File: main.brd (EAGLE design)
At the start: 43.4 x 29.3 mm, 26 parts, among them IC1 FT232RL, U1 ATMEGA328P_TQFP, Y3 16MHz

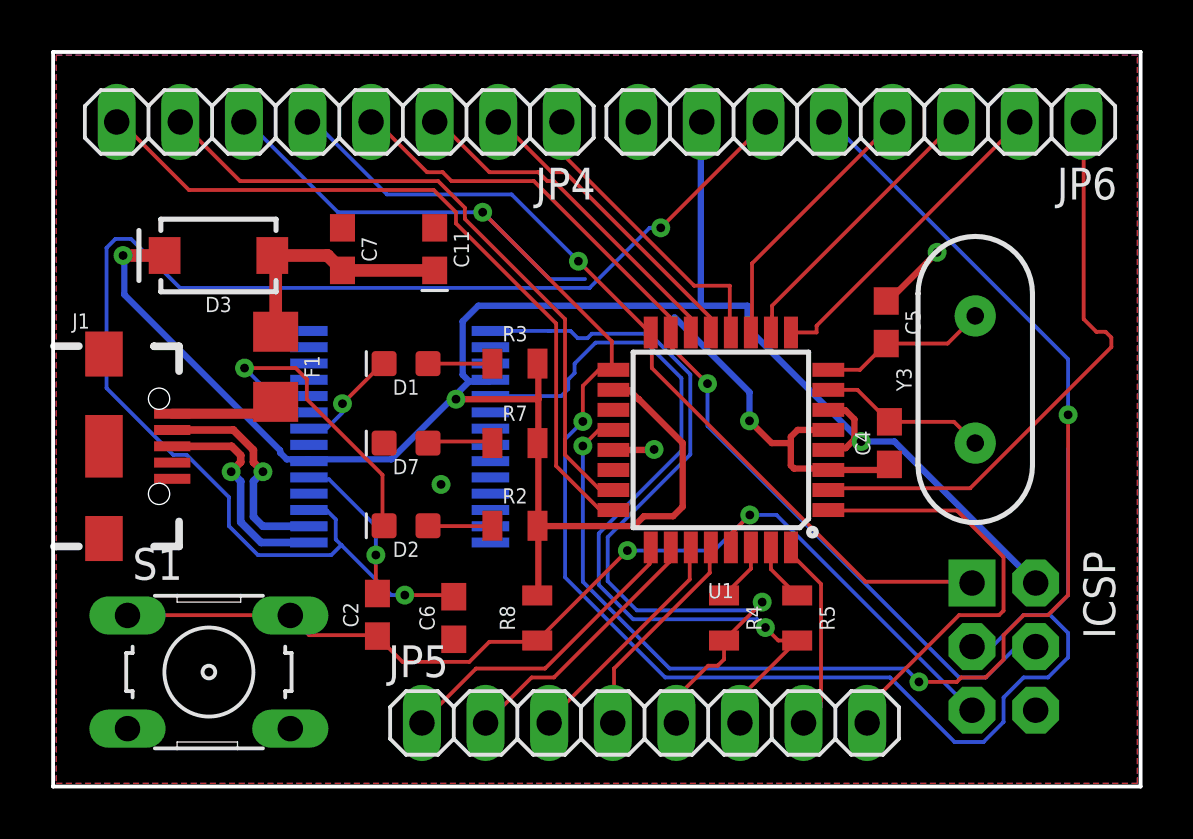
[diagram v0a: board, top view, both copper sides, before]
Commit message: 8/1/17 - Used new ATMEGA32U4
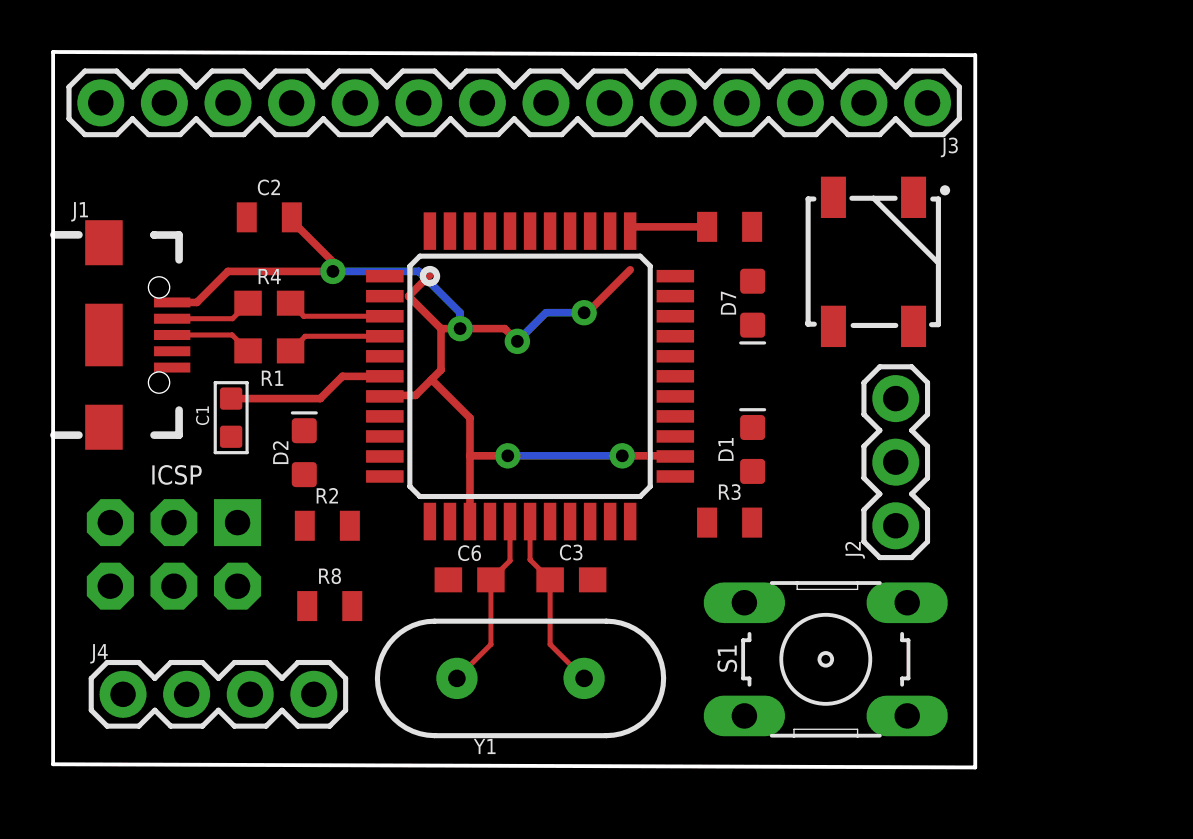
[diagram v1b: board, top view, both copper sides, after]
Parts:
- removed C11: 4.7uF, SparkFun-Capacitors:0603-POLAR
- removed C4, C5: 22pF, SparkFun-Capacitors:0603
- removed C7: 0.1uF, SparkFun-Capacitors:0603
- removed F1: 6V/0.5A, SparkFun-Fuses:1206
- removed IC1: FT232RL, ftdichip:SSOP28
- removed JP4, JP5, JP6: (no value), pinhead:1X08
- removed R5: 1k, SparkFun-Resistors:0805
- removed U1: ATMEGA328P_TQFP, SparkFun-IC-Microcontroller:TQFP32-08
- removed Y3: 16MHz, SparkFun-Clocks:HC49US
- added C1: 1uf, Seeed-Capacitor:C0603
- added C3: 22pF, SparkFun-Capacitors:0603
- added J2: (no value), SparkFun-Connectors:1X03
- added J3: (no value), SparkFun-Connectors:1X14
- added J4: (no value), SparkFun-Connectors:1X04
- added R1: 22, SparkFun-Resistors:0603
- added U$1: 32U4, SparkFun-IC-Microcontroller:TQFP44
- added Y1: 16MHz, SparkFun-Clocks:HC49US
- C2: value 0.1uF -> 10uF; device SparkFun-Capacitors:0603 -> SparkFun-Capacitors:0805
- C6: value 0.1uF -> 22pF
- D3: value 2A/100V/850mV -> WS2812B; device SparkFun-DiscreteSemi:SMA-DIODE -> SparkFun-LED:WS2812B
- R4: value 1k -> 22; device SparkFun-Resistors:0805 -> SparkFun-Resistors:0603
- moved ICSP 33.4 mm to (4.83, 11.9), turned to 180 degrees
- moved D3 26.2 mm to (32.8, 23.6), turned to 270 degrees
- moved S1 24.6 mm to (30.9, 7.75), turned to 180 degrees
- moved R4 22.1 mm to (8.64, 22.0), turned to 0 degrees
- moved C2 16.5 mm to (8.64, 25.4), turned to 0 degrees
- moved D7 14.9 mm to (27.9, 22.0), turned to 270 degrees
- moved D1 14.3 mm to (27.9, 16.1), turned to 90 degrees
- moved R7 12.2 mm to (27.0, 25.0), turned to 180 degrees
- moved R3 10.7 mm to (27.0, 13.2), turned to 180 degrees
- moved R8 8.30 mm to (11.0, 9.87), turned to 0 degrees
- moved R2 7.49 mm to (11.0, 13.1)
- moved D2 5.00 mm to (10.0, 16.0), turned to 90 degrees
- moved J1 4.45 mm to (2.03, 20.7)
- moved C6 1.65 mm to (16.6, 10.9), turned to 0 degrees
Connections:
- removed net 3.3V: C6.2, IC1.17, JP6.6
- removed net CBUS0: D2.C, IC1.23
- removed net CBUS1: D1.C, IC1.22
- removed net N$7: C2.2, IC1.19
- removed net PB0: JP4.1, U1.12
- removed net PB1: JP4.2, U1.13
- removed net PB2: JP4.3, U1.14
- removed net PC0: JP4.7, U1.23
- removed net PC1: JP4.8, U1.24
- removed net PC2: JP5.1, U1.25
- removed net PC3: JP5.2, U1.26
- removed net PC4: JP5.3, U1.27
- removed net PC5: JP5.4, U1.28
- removed net PD2: JP5.7, U1.32
- removed net PD3: JP5.8, U1.1
- removed net PD5: JP6.2, U1.9
- removed net RX_1_N: IC1.5, JP5.6, R5.2
- removed net RX_1_P: IC1.1, JP5.5, R4.2
- removed net VBUS: F1.2, J1.VBUS
- removed net V_USB: C11.+, C7.2, D3.A, F1.1
- new net PB4: J3.1, U$1.28
- new net PB5: D3.4, J3.2, U$1.29
- new net PB6: J3.3, U$1.30
- new net PB7: U$1.12
- new net PC6: J3.4, U$1.31
- new net PC7: J3.5, U$1.32
- new net PD0: J4.1, U$1.18
- new net PD1: J4.2, U$1.19
- new net PE6: U$1.1
- new net PF0: J3.11, U$1.41
- new net PF1: J3.10, U$1.40
- new net PF4: J3.9, U$1.39
- new net PF5: J3.8, U$1.38
- new net PF6: J3.7, U$1.37
- new net PF7: J3.6, U$1.36
- new net RX_LED: R2.2, U$1.8
- new net TX_LED: R3.2, U$1.22
- new net UCAP: C1.1, U$1.6
- new net USBD1_N: R4.2, U$1.3
- new net USBD1_P: R1.2, U$1.4
- net 5V: now also C2.2, D3.1, J1.VBUS, J3.14, U$1.14, U$1.2, U$1.24, U$1.34, U$1.44, U$1.7; no longer D3.C, IC1.20, IC1.4, JP6.7, R2.2, R3.2, U1.18, U1.4, U1.6
- net AREF: now also J3.12, U$1.42; no longer JP6.5, U1.20
- net GND: now also C1.2, C2.1, C3.1, D1.C, D2.C, D3.3, J3.13, U$1.15, U$1.23, U$1.33, U$1.35, U$1.43, U$1.5; no longer C11.-, C4.1, C5.1, C7.1, IC1.18, IC1.21, IC1.25, IC1.26, IC1.7, JP6.8, U1.21, U1.3, U1.5
- net MISO: now also U$1.11; no longer JP4.5, U1.16
- net MOSI: now also U$1.10; no longer JP4.4, U1.15
- net PD4: now also J2.1, U$1.25; no longer JP6.1, U1.2
- net PD6: now also J2.2, U$1.26; no longer JP6.3, U1.10
- net PD7: now also J2.3, U$1.27; no longer JP6.4, U1.11
- net RST: now also U$1.13; no longer C2.1, U1.29
- net RX_N: now also J4.4, U$1.21; no longer R5.1, U1.31
- net RX_P: now also J4.3, U$1.20; no longer R4.1, U1.30
- net SCK: now also U$1.9; no longer JP4.6, U1.17
- net USBD_N: now also R4.1; no longer IC1.16
- net USBD_P: now also R1.1; no longer IC1.15
- net XTAL_N: now also C6.2, U$1.16, Y1.2; no longer C5.2, U1.8, Y3.2
- net XTAL_P: now also C3.2, U$1.17, Y1.1; no longer C4.2, U1.7, Y3.1
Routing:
- net SCK: track 71.5 -> 0.00 mm, vias 2 -> 0
- net 3.3V: track 56.4 -> 0.00 mm, vias 2 -> 0
- net AREF: track 52.9 -> 0.00 mm, vias 3 -> 0
- net RST: track 41.8 -> 0.00 mm, vias 2 -> 0
- net 5V: track 88.8 -> 49.7 mm, vias 3 -> 6
- net MOSI: track 38.0 -> 0.00 mm, vias 1 -> 0
- net MISO: track 35.0 -> 0.00 mm, vias 1 -> 0
- net RX_1_P: track 32.3 -> 0.00 mm, vias 1 -> 0
- net RX_1_N: track 32.3 -> 0.00 mm, vias 1 -> 0
- net PC1: track 29.9 -> 0.00 mm
- net PC0: track 26.8 -> 0.00 mm
- net PD4: track 23.3 -> 0.00 mm
- net GND: track 18.8 -> 0.00 mm, vias 4 -> 0
- net PD3: track 17.6 -> 0.00 mm
- net PB2: track 14.1 -> 0.00 mm
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- removed copper zone on layer 1, net GND
- removed copper zone on layer 16, net GND
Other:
- board size 43.4 x 29.3 mm -> 36.8 x 28.6 mm

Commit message: Move vias
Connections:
- net RX_N renamed TX
- net RX_P renamed RX
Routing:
- net 5V: track 49.7 -> 54.7 mm, vias 6 -> 5
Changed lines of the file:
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@@
 <via x="11.176" y="23.241" extent="1-16" drill="0.508"/>
 <wire x1="11.176" y1="23.241" x2="14.605" y2="23.241" width="0.3048" layer="16"/>
-<wire x1="14.605" y1="23.241" x2="16.256" y2="21.59" width="0.3048" layer="16"/>
-<wire x1="16.256" y1="21.59" x2="16.256" y2="20.955" width="0.3048" layer="16"/>
-<via x="16.256" y="20.955" extent="1-16" drill="0.508"/>
+<wire x1="16.256" y1="21.59" x2="14.605" y2="23.241" width="0.3048" layer="16"/>
 <wire x1="14.199" y1="22.25" x2="15.494" y2="20.955" width="0.3048" layer="1"/>
-<wire x1="15.494" y1="20.955" x2="16.256" y2="20.955" width="0.3048" layer="1"/>
-<wire x1="15.494" y1="20.955" x2="15.494" y2="19.304" width="0.3048" layer="1"/>
-<wire x1="15.494" y1="19.304" x2="14.478" y2="18.288" width="0.3048" layer="1"/>
-<wire x1="14.478" y1="18.288" x2="13.288" y2="18.288" width="0.3048" layer="1"/>
-<wire x1="15.05" y1="23.101" x2="14.199" y2="22.25" width="0.3048" layer="1"/>
-<wire x1="23.05" y1="23.304" x2="21.336" y2="21.59" width="0.3048" layer="1"/>
-<wire x1="21.336" y1="21.59" x2="21.209" y2="21.59" width="0.3048" layer="1"/>
-<via x="21.209" y="21.59" extent="1-16" drill="0.508"/>
-<wire x1="21.209" y1="21.59" x2="19.685" y2="21.59" width="0.3048" layer="16"/>
-<wire x1="19.685" y1="21.59" x2="18.542" y2="20.447" width="0.3048" layer="16"/>
-<via x="18.542" y="20.447" extent="1-16" drill="0.508"/>
-<wire x1="16.256" y1="20.955" x2="18.034" y2="20.955" width="0.3048" layer="1"/>
-<wire x1="18.034" y1="20.955" x2="18.542" y2="20.447" width="0.3048" layer="1"/>
 <wire x1="11.176" y1="23.622" x2="11.176" y2="23.241" width="0.3048" layer="1"/>
 <wire x1="9.536" y1="25.262" x2="11.176" y2="23.622" width="0.3048" layer="1"/>
@@
 <contactref element="U$1" pad="24"/>
 <contactref element="U$1" pad="44"/>
-<wire x1="15.113" y1="18.923" x2="16.65" y2="17.386" width="0.3048" layer="1"/>
-<wire x1="16.65" y1="15.87493125" x2="16.65" y2="13.25" width="0.3048" layer="1"/>
-<wire x1="16.65" y1="15.87493125" x2="16.65" y2="17.386" width="0.3048" layer="1"/>
-<wire x1="24.825" y1="15.875" x2="24.85" y2="15.85" width="0.3048" layer="1"/>
-<wire x1="24.825" y1="15.875" x2="22.733" y2="15.875" width="0.3048" layer="1"/>
-<via x="22.733" y="15.875" extent="1-16" drill="0.508"/>
-<wire x1="22.733" y1="15.875" x2="18.161" y2="15.875" width="0.3048" layer="16"/>
-<via x="18.161" y="15.875" extent="1-16" drill="0.508"/>
-<wire x1="18.161" y1="15.875" x2="18.16093125" y2="15.87493125" width="0.3048" layer="1"/>
-<wire x1="18.16093125" y1="15.87493125" x2="16.65" y2="15.87493125" width="0.3048" layer="1"/>
+<wire x1="16.65" y1="17.39893125" x2="16.65" y2="13.25" width="0.3048" layer="1"/>
+<wire x1="24.85" y1="15.85" x2="24.825" y2="15.875" width="0.3048" layer="1"/>
+<via x="21.844" y="17.399" extent="1-16" drill="0.508"/>
+<via x="18.542" y="17.399" extent="1-16" drill="0.508"/>
 <contactref element="U$1" pad="7"/>
 <contactref element="U$1" pad="2"/>
 <contactref element="C2" pad="2"/>
 <contactref element="J3" pad="14"/>
+<wire x1="18.542" y1="17.399" x2="18.54193125" y2="17.39893125" width="0.3048" layer="1"/>
+<wire x1="16.65" y1="17.39893125" x2="18.54193125" y2="17.39893125" width="0.3048" layer="1"/>
+<wire x1="18.542" y1="17.399" x2="21.844" y2="17.399" width="0.3048" layer="16"/>
+<wire x1="21.844" y1="17.399" x2="23.393" y2="15.85" width="0.3048" layer="1"/>
+<wire x1="23.393" y1="15.85" x2="24.85" y2="15.85" width="0.3048" layer="1"/>
+<wire x1="14.199" y1="22.25" x2="13.25" y2="22.25" width="0.3048" layer="1"/>
+<wire x1="15.494" y1="20.955" x2="19.177" y2="20.955" width="0.3048" layer="1"/>
+<via x="19.177" y="20.955" extent="1-16" drill="0.35"/>
+<wire x1="18.542" y1="21.59" x2="19.177" y2="20.955" width="0.3048" layer="16"/>
+<wire x1="18.542" y1="21.59" x2="16.256" y2="21.59" width="0.3048" layer="16"/>
+<wire x1="15.76093125" y1="18.288" x2="16.65" y2="17.39893125" width="0.3048" layer="1"/>
+<wire x1="13.288" y1="18.288" x2="15.76093125" y2="18.288" width="0.3048" layer="1"/>
+<wire x1="19.177" y1="20.955" x2="19.177" y2="18.034" width="0.3048" layer="1"/>
+<wire x1="19.177" y1="18.034" x2="18.542" y2="17.399" width="0.3048" layer="1"/>
+<wire x1="19.177" y1="20.955" x2="20.32" y2="20.955" width="0.3048" layer="16"/>
+<wire x1="20.32" y1="20.955" x2="21.59" y2="22.225" width="0.3048" layer="16"/>
+<via x="21.59" y="22.225" extent="1-16" drill="0.35"/>
+<wire x1="21.59" y1="22.225" x2="23.05" y2="23.685" width="0.3048" layer="1"/>
+<wire x1="23.05" y1="23.685" x2="23.05" y2="24.85" width="0.3048" layer="1"/>
 <wire x1="26.11925" y1="25.019" x2="31.166" y2="21.045" width="0" layer="19" extent="1-1"/>
 <wire x1="23.05" y1="24.85" x2="23.219" y2="25.019" width="0" layer="19" extent="1-1"/>
-<wire x1="23.05" y1="23.304" x2="23.05" y2="24.85" width="0" layer="19" extent="1-1"/>
 <wire x1="13.25" y1="18.25" x2="13.288" y2="18.288" width="0" layer="19" extent="1-1"/>
 <wire x1="9.536" y1="25.4" x2="9.536" y2="25.262" width="0" layer="19" extent="1-1"/>
-<wire x1="15.113" y1="18.923" x2="15.494" y2="19.304" width="0" layer="19" extent="1-1"/>
-<wire x1="13.25" y1="22.25" x2="14.199" y2="22.25" width="0" layer="19" extent="1-1"/>
 <wire x1="15.05" y1="24.85" x2="14.605" y2="23.241" width="0" layer="19" extent="1-16"/>
 <wire x1="11.949" y1="9.87425" x2="16.65" y2="13.25" width="0" layer="19" extent="1-1"/>
@@
 <wire x1="13.25" y1="21.45" x2="10.007" y2="21.45" width="0.2032" layer="1"/>
 <wire x1="10.007" y1="21.45" x2="9.486" y2="21.971" width="0.2032" layer="1"/>
-</signal>
-<signal name="RX_P">
-<contactref element="U$1" pad="20"/>
-<contactref element="J4" pad="3"/>
-<wire x1="7.874" y1="6.35" x2="21.45" y2="13.25" width="0" layer="19" extent="1-1"/>
-</signal>
-<signal name="RX_N">
-<contactref element="U$1" pad="21"/>
-<contactref element="J4" pad="4"/>
-<wire x1="10.414" y1="6.35" x2="22.25" y2="13.25" width="0" layer="19" extent="1-1"/>
 </signal>
 <signal name="PC7">
@@
 <wire x1="24.85" y1="21.45" x2="27.305" y2="29.972" width="0" layer="19" extent="1-1"/>
 </signal>
+<signal name="RX">
+<contactref element="U$1" pad="20"/>
+<contactref element="J4" pad="3"/>
+<wire x1="7.874" y1="6.35" x2="21.45" y2="13.25" width="0" layer="19" extent="1-1"/>
+</signal>
+<signal name="TX">
+<contactref element="U$1" pad="21"/>
+<contactref element="J4" pad="4"/>
+<wire x1="10.414" y1="6.35" x2="22.25" y2="13.25" width="0" layer="19" extent="1-1"/>
+</signal>
 </signals>

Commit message: AutoRouter +Text
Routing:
- net 5V: track 54.7 -> 112.7 mm, vias 5 -> 6
- net RST: track 0.00 -> 47.3 mm
- net PD0: track 0.00 -> 25.4 mm, vias 0 -> 1
- net RX: track 0.00 -> 23.6 mm, vias 0 -> 1
- net PD1: track 0.00 -> 21.6 mm, vias 0 -> 1
- net TX: track 0.00 -> 19.3 mm
- net PB4: track 0.00 -> 19.0 mm
- net PB5: track 0.00 -> 17.0 mm
- net SCK: track 0.00 -> 14.2 mm, vias 0 -> 1
- net PB6: track 0.00 -> 12.8 mm
- net AREF: track 0.00 -> 12.2 mm
- net MOSI: track 0.00 -> 12.1 mm
- net PF0: track 0.00 -> 10.5 mm
- net PD4: track 0.00 -> 10.3 mm
- net PC6: track 0.00 -> 9.99 mm
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- added copper zone on layer 1, net GND
- added copper zone on layer 16, net GND
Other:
- outline, holes or cut-outs redrawn
- board text added: "5V"
- board text added: "AREF"
- board text added: "GND"
- board text added: "MISO"
- board text added: "MOSI"
- board text added: "PB4"
- board text added: "PB5"
- board text added: "PB6"
- board text added: "PC6"
- board text added: "PC7"
- board text added: "PD4"
- board text added: "PD6"
- board text added: "PD7"
- board text added: "PF0"
- board text added: "PF1"
- board text added: "PF4"
- board text added: "PF5"
- board text added: "PF6"
- board text added: "PF7"
- board text added: "RST"
- board text added: "RX"
- board text added: "SCK"
- board text added: "SCL"
- board text added: "SDA"
- board text added: "TX"
